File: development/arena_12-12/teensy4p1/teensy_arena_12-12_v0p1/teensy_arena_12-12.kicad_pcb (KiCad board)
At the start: 6 copper layers, 228.6 x 228.6 mm, 434 parts, among them J1 Barrel_Jack, J2 Conn_01x04, J3 Conn_01x04, J4 Barrel_Jack, P1 CONN15, P10 CONN15, P11 CONN15, P12 CONN15, P2 CONN15, P3 CONN15, P4 CONN15, P5 CONN15, P6 CONN15, P7 CONN15, P8 CONN15, P9 CONN15, Q1 MOSFET_NCHAN, SW1 SW_SPDT, U1 Teensy4.1, U10 TXB0108PW, U11 TXB0108PW, U12 TXB0108PW, U13 TXB0108PW, U14 TXB0108PW, U15 74LVC1G17, U16 74LVC1G17, U17 74LVC1G17, U18 74LVC1G17, U19 74LVC2G17, U2 74LVC2G17, U20 74LVC2G17, U21 74LVC2G17, U22 74LVC2G17, U23 74LVC2G17, U24 74LVC2G17, U25 74LVC2G17, U26 74LVC2G17, U27 74LVC2G17, U28 74LVC2G17, U29 74LVC2G17, U3 TXB0108PW, U30 74LVC2G17, U31 74LVC2G17, U32 74LVC2G17, U33 74LVC2G17, U34 74LVC2G17, U35 74LVC2G17, U36 74LVC2G17, U37 74LVC2G17, U38 74LVC2G17, U39 74LVC2G17, U4 TXB0108PW, U40 74LVC2G17, U41 74LVC2G17, U42 74LVC2G17, U43 74LVC2G17, U44 74LVC2G17, U45 74LVC2G17, U46 74LVC2G17, U47 74LVC2G17, U48 74LVC2G17, U49 74LVC2G17, U5 TXB0108PW, U50 74LVC2G17, U51 74LVC2G17, U52 74LVC2G17, U53 74LVC2G17, U54 74LVC2G17, U55 74LVC2G17, U56 74LVC2G17, U57 74LVC2G17, U58 74LVC2G17, U59 74LVC2G17, U6 TXB0108PW, U60 74LVC2G17, U61 74LVC2G17, U62 74LVC2G17, U63 74LVC2G17, U64 74LVC2G17, U65 74LVC2G17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

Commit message: Worked on 12-12 arena layout.
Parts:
- removed the Q1 at (284.3, 131.0)
- added R223: 68, Resistor_SMD:R_0603_1608Metric, F.Cu at (272.5, 172.7)
- added R224: 68, Resistor_SMD:R_0603_1608Metric, F.Cu at (257.2, 126.0)
- added R225: 68, Resistor_SMD:R_0603_1608Metric, F.Cu at (220.7, 93.3)
- added R226: 68, Resistor_SMD:R_0603_1608Metric, F.Cu at (172.7, 83.1)
- added R227: 68, Resistor_SMD:R_0603_1608Metric, F.Cu at (126.0, 98.4)
- added R228: 68, Resistor_SMD:R_0603_1608Metric, F.Cu at (93.3, 134.9)
- added R229: 68, Resistor_SMD:R_0603_1608Metric, F.Cu at (83.1, 182.9)
- added R230: 68, Resistor_SMD:R_0603_1608Metric, F.Cu at (98.4, 229.6)
- added R231: 68, Resistor_SMD:R_0603_1608Metric, F.Cu at (134.9, 262.3)
- added R232: 68, Resistor_SMD:R_0603_1608Metric, F.Cu at (182.9, 272.5)
- added R233: 68, Resistor_SMD:R_0603_1608Metric, F.Cu at (229.6, 257.2)
- added R234: 68, Resistor_SMD:R_0603_1608Metric, F.Cu at (262.3, 220.7)
- moved C50 361.1 mm to (272.5, 187.0), turned to 180 degrees
- moved C49 360.2 mm to (272.4, 181.6), turned to 180 degrees
- moved C48 359.4 mm to (272.4, 176.3), turned to 180 degrees
- moved C47 358.0 mm to (272.5, 169.0), turned to 180 degrees
- moved C91 349.8 mm to (264.2, 217.5), turned to 150 degrees
- moved R130 349.1 mm to (272.5, 178.0)
- moved R131 349.0 mm to (272.4, 180.0)
- moved C92 347.7 mm to (260.5, 223.9), turned to 150 degrees
- moved C93 346.0 mm to (257.9, 228.4), turned to 150 degrees
- moved C94 344.3 mm to (255.1, 233.1), turned to 150 degrees
- moved R128 342.0 mm to (272.5, 170.6)
- moved R127 341.9 mm to (272.5, 167.4)
- moved C87 341.6 mm to (232.7, 255.4), turned to 120 degrees
- moved C54 340.0 mm to (264.4, 138.5), turned to -150 degrees
- moved R215 337.6 mm to (265.0, 216.2), turned to -30 degrees
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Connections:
- P1 pad 6: /Level Shifters/PAN5V.MISO_0 -> /Panel Headers/HDR_MISO_0_P1
- P10 pad 6: /Level Shifters/PAN5V.MISO_1 -> /Panel Headers/HDR_MISO_1_P10
- P11 pad 6: /Level Shifters/PAN5V.MISO_1 -> /Panel Headers/HDR_MISO_1_P11
- P12 pad 6: /Level Shifters/PAN5V.MISO_1 -> /Panel Headers/HDR_MISO_1_P12
- P2 pad 6: /Level Shifters/PAN5V.MISO_0 -> /Panel Headers/HDR_MISO_0_P2
- P3 pad 6: /Level Shifters/PAN5V.MISO_0 -> /Panel Headers/HDR_MISO_0_P3
- P4 pad 6: /Level Shifters/PAN5V.MISO_0 -> /Panel Headers/HDR_MISO_0_P4
- P5 pad 6: /Level Shifters/PAN5V.MISO_0 -> /Panel Headers/HDR_MISO_0_P5
- P6 pad 6: /Level Shifters/PAN5V.MISO_0 -> /Panel Headers/HDR_MISO_0_P6
- P7 pad 6: /Level Shifters/PAN5V.MISO_1 -> /Panel Headers/HDR_MISO_1_P7
- P8 pad 6: /Level Shifters/PAN5V.MISO_1 -> /Panel Headers/HDR_MISO_1_P8
- P9 pad 6: /Level Shifters/PAN5V.MISO_1 -> /Panel Headers/HDR_MISO_1_P9
- U36 pad 1: /Level Shifters/PAN5V.SCK_0_P1 -> /Level Shifters/PAN5V.MOSI_0_P1
- U36 pad 3: /Level Shifters/PAN5V.MOSI_0_P1 -> /Level Shifters/PAN5V.SCK_0_P1
- U36 pad 4: Net-(R128-Pad2) -> Net-(R127-Pad2)
- U36 pad 6: Net-(R127-Pad2) -> Net-(R128-Pad2)
- U37 pad 1: /Level Shifters/PAN5V.CS_00_P1 -> /Level Shifters/PAN5V.CS_01_P1
- U37 pad 3: /Level Shifters/PAN5V.CS_01_P1 -> /Level Shifters/PAN5V.CS_00_P1
- U37 pad 4: Net-(R130-Pad2) -> Net-(R129-Pad2)
- U37 pad 6: Net-(R129-Pad2) -> Net-(R130-Pad2)
- U38 pad 1: /Level Shifters/PAN5V.CS_02_P1 -> /Level Shifters/PAN5V.CS_03_P1
- U38 pad 3: /Level Shifters/PAN5V.CS_03_P1 -> /Level Shifters/PAN5V.CS_02_P1
- U38 pad 4: Net-(R132-Pad2) -> Net-(R131-Pad2)
- U38 pad 6: Net-(R131-Pad2) -> Net-(R132-Pad2)
- U39 pad 1: /Level Shifters/PAN5V.CS_04_P1 -> /Level Shifters/PAN5V.EXT_INT
- U39 pad 3: /Level Shifters/PAN5V.EXT_INT -> /Level Shifters/PAN5V.CS_04_P1
- U39 pad 4: Net-(R134-Pad2) -> Net-(R133-Pad2)
- U39 pad 6: Net-(R133-Pad2) -> Net-(R134-Pad2)
- U40 pad 1: /Level Shifters/PAN5V.SCK_0_P2 -> /Level Shifters/PAN5V.MOSI_0_P2
- U40 pad 3: /Level Shifters/PAN5V.MOSI_0_P2 -> /Level Shifters/PAN5V.SCK_0_P2
- U40 pad 4: Net-(R136-Pad2) -> Net-(R135-Pad2)
- U40 pad 6: Net-(R135-Pad2) -> Net-(R136-Pad2)
- U41 pad 1: /Level Shifters/PAN5V.CS_05_P2 -> /Level Shifters/PAN5V.CS_06_P2
- U41 pad 3: /Level Shifters/PAN5V.CS_06_P2 -> /Level Shifters/PAN5V.CS_05_P2
- U41 pad 4: Net-(R138-Pad2) -> Net-(R137-Pad2)
- U41 pad 6: Net-(R137-Pad2) -> Net-(R138-Pad2)
- U42 pad 1: /Level Shifters/PAN5V.CS_07_P2 -> /Level Shifters/PAN5V.CS_08_P2
- U42 pad 3: /Level Shifters/PAN5V.CS_08_P2 -> /Level Shifters/PAN5V.CS_07_P2
- U42 pad 4: Net-(R140-Pad2) -> Net-(R139-Pad2)
- U42 pad 6: Net-(R139-Pad2) -> Net-(R140-Pad2)
- U43 pad 1: /Level Shifters/PAN5V.CS_09_P2 -> /Level Shifters/PAN5V.EXT_INT
- U43 pad 3: /Level Shifters/PAN5V.EXT_INT -> /Level Shifters/PAN5V.CS_09_P2
- U43 pad 4: Net-(R142-Pad2) -> Net-(R141-Pad2)
- U43 pad 6: Net-(R141-Pad2) -> Net-(R142-Pad2)
- U44 pad 1: /Level Shifters/PAN5V.SCK_0_P3 -> /Level Shifters/PAN5V.MOSI_0_P3
- U44 pad 3: /Level Shifters/PAN5V.MOSI_0_P3 -> /Level Shifters/PAN5V.SCK_0_P3
- U44 pad 4: Net-(R144-Pad2) -> Net-(R143-Pad2)
- U44 pad 6: Net-(R143-Pad2) -> Net-(R144-Pad2)
- U45 pad 1: /Level Shifters/PAN5V.CS_10_P3 -> /Level Shifters/PAN5V.CS_11_P3
- U45 pad 3: /Level Shifters/PAN5V.CS_11_P3 -> /Level Shifters/PAN5V.CS_10_P3
- U45 pad 4: Net-(R146-Pad2) -> Net-(R145-Pad2)
- U45 pad 6: Net-(R145-Pad2) -> Net-(R146-Pad2)
- U46 pad 1: /Level Shifters/PAN5V.CS_12_P3 -> /Level Shifters/PAN5V.CS_13_P3
- U46 pad 3: /Level Shifters/PAN5V.CS_13_P3 -> /Level Shifters/PAN5V.CS_12_P3
- U46 pad 4: Net-(R148-Pad2) -> Net-(R147-Pad2)
- U46 pad 6: Net-(R147-Pad2) -> Net-(R148-Pad2)
- U47 pad 1: /Level Shifters/PAN5V.CS_14_P3 -> /Level Shifters/PAN5V.EXT_INT
- U47 pad 3: /Level Shifters/PAN5V.EXT_INT -> /Level Shifters/PAN5V.CS_14_P3
- U47 pad 4: Net-(R150-Pad2) -> Net-(R149-Pad2)
- U47 pad 6: Net-(R149-Pad2) -> Net-(R150-Pad2)
- U48 pad 1: /Level Shifters/PAN5V.SCK_0_P4 -> /Level Shifters/PAN5V.MOSI_0_P4
- U48 pad 3: /Level Shifters/PAN5V.MOSI_0_P4 -> /Level Shifters/PAN5V.SCK_0_P4
- U48 pad 4: Net-(R152-Pad2) -> Net-(R151-Pad2)
- U48 pad 6: Net-(R151-Pad2) -> Net-(R152-Pad2)
- U49 pad 1: /Level Shifters/PAN5V.CS_15_P4 -> /Level Shifters/PAN5V.CS_16_P4
- U49 pad 3: /Level Shifters/PAN5V.CS_16_P4 -> /Level Shifters/PAN5V.CS_15_P4
- U49 pad 4: Net-(R154-Pad2) -> Net-(R153-Pad2)
- U49 pad 6: Net-(R153-Pad2) -> Net-(R154-Pad2)
- U50 pad 1: /Level Shifters/PAN5V.CS_17_P4 -> /Level Shifters/PAN5V.CS_18_P4
- U50 pad 3: /Level Shifters/PAN5V.CS_18_P4 -> /Level Shifters/PAN5V.CS_17_P4
- U50 pad 4: Net-(R156-Pad2) -> Net-(R155-Pad2)
- U50 pad 6: Net-(R155-Pad2) -> Net-(R156-Pad2)
- U51 pad 1: /Level Shifters/PAN5V.CS_19_P4 -> /Level Shifters/PAN5V.EXT_INT
- U51 pad 3: /Level Shifters/PAN5V.EXT_INT -> /Level Shifters/PAN5V.CS_19_P4
- U51 pad 4: Net-(R158-Pad2) -> Net-(R157-Pad2)
- U51 pad 6: Net-(R157-Pad2) -> Net-(R158-Pad2)
- U52 pad 1: /Level Shifters/PAN5V.SCK_0_P5 -> /Level Shifters/PAN5V.MOSI_0_P5
- U52 pad 3: /Level Shifters/PAN5V.MOSI_0_P5 -> /Level Shifters/PAN5V.SCK_0_P5
- U52 pad 4: Net-(R160-Pad2) -> Net-(R159-Pad2)
- U52 pad 6: Net-(R159-Pad2) -> Net-(R160-Pad2)
- U53 pad 1: /Level Shifters/PAN5V.CS_20_P5 -> /Level Shifters/PAN5V.CS_21_P5
- U53 pad 3: /Level Shifters/PAN5V.CS_21_P5 -> /Level Shifters/PAN5V.CS_20_P5
- U53 pad 4: Net-(R162-Pad2) -> Net-(R161-Pad2)
- U53 pad 6: Net-(R161-Pad2) -> Net-(R162-Pad2)
- U54 pad 1: /Level Shifters/PAN5V.CS_22_P5 -> /Level Shifters/PAN5V.CS_23_P5
- U54 pad 3: /Level Shifters/PAN5V.CS_23_P5 -> /Level Shifters/PAN5V.CS_22_P5
- U54 pad 4: Net-(R164-Pad2) -> Net-(R163-Pad2)
- U54 pad 6: Net-(R163-Pad2) -> Net-(R164-Pad2)
- U55 pad 1: /Level Shifters/PAN5V.CS_24_P5 -> /Level Shifters/PAN5V.EXT_INT
- U55 pad 3: /Level Shifters/PAN5V.EXT_INT -> /Level Shifters/PAN5V.CS_24_P5
- U55 pad 4: Net-(R166-Pad2) -> Net-(R165-Pad2)
- U55 pad 6: Net-(R165-Pad2) -> Net-(R166-Pad2)
- U56 pad 1: /Level Shifters/PAN5V.SCK_0_P6 -> /Level Shifters/PAN5V.MOSI_0_P6
- U56 pad 3: /Level Shifters/PAN5V.MOSI_0_P6 -> /Level Shifters/PAN5V.SCK_0_P6
- U56 pad 4: Net-(R168-Pad2) -> Net-(R167-Pad2)
- U56 pad 6: Net-(R167-Pad2) -> Net-(R168-Pad2)
- U57 pad 1: /Level Shifters/PAN5V.CS_25_P6 -> /Level Shifters/PAN5V.CS_26_P6
- U57 pad 3: /Level Shifters/PAN5V.CS_26_P6 -> /Level Shifters/PAN5V.CS_25_P6
- U57 pad 4: Net-(R170-Pad2) -> Net-(R169-Pad2)
- U57 pad 6: Net-(R169-Pad2) -> Net-(R170-Pad2)
- U58 pad 1: /Level Shifters/PAN5V.CS_27_P6 -> /Level Shifters/PAN5V.CS_28_P6
- U58 pad 3: /Level Shifters/PAN5V.CS_28_P6 -> /Level Shifters/PAN5V.CS_27_P6
- U58 pad 4: Net-(R172-Pad2) -> Net-(R171-Pad2)
- U58 pad 6: Net-(R171-Pad2) -> Net-(R172-Pad2)
- U59 pad 1: /Level Shifters/PAN5V.CS_29_P6 -> /Level Shifters/PAN5V.EXT_INT
- U59 pad 3: /Level Shifters/PAN5V.EXT_INT -> /Level Shifters/PAN5V.CS_29_P6
- U59 pad 4: Net-(R174-Pad2) -> Net-(R173-Pad2)
- U59 pad 6: Net-(R173-Pad2) -> Net-(R174-Pad2)
- U60 pad 1: /Level Shifters/PAN5V.SCK_1_P7 -> /Level Shifters/PAN5V.MOSI_1_P7
- U60 pad 3: /Level Shifters/PAN5V.MOSI_1_P7 -> /Level Shifters/PAN5V.SCK_1_P7
- U60 pad 4: Net-(R176-Pad2) -> Net-(R175-Pad2)
- U60 pad 6: Net-(R175-Pad2) -> Net-(R176-Pad2)
- U61 pad 1: /Level Shifters/PAN5V.CS_00_P7 -> /Level Shifters/PAN5V.CS_01_P7
- U61 pad 3: /Level Shifters/PAN5V.CS_01_P7 -> /Level Shifters/PAN5V.CS_00_P7
- U61 pad 4: Net-(R178-Pad2) -> Net-(R177-Pad2)
- U61 pad 6: Net-(R177-Pad2) -> Net-(R178-Pad2)
- U62 pad 1: /Level Shifters/PAN5V.CS_02_P7 -> /Level Shifters/PAN5V.CS_03_P7
- U62 pad 3: /Level Shifters/PAN5V.CS_03_P7 -> /Level Shifters/PAN5V.CS_02_P7
- U62 pad 4: Net-(R180-Pad2) -> Net-(R179-Pad2)
- U62 pad 6: Net-(R179-Pad2) -> Net-(R180-Pad2)
- U63 pad 1: /Level Shifters/PAN5V.CS_04_P7 -> /Level Shifters/PAN5V.EXT_INT
- U63 pad 3: /Level Shifters/PAN5V.EXT_INT -> /Level Shifters/PAN5V.CS_04_P7
- U63 pad 4: Net-(R182-Pad2) -> Net-(R181-Pad2)
- U63 pad 6: Net-(R181-Pad2) -> Net-(R182-Pad2)
- U64 pad 1: /Level Shifters/PAN5V.SCK_1_P8 -> /Level Shifters/PAN5V.MOSI_1_P8
- U64 pad 3: /Level Shifters/PAN5V.MOSI_1_P8 -> /Level Shifters/PAN5V.SCK_1_P8
- U64 pad 4: Net-(R184-Pad2) -> Net-(R183-Pad2)
- U64 pad 6: Net-(R183-Pad2) -> Net-(R184-Pad2)
- U65 pad 1: /Level Shifters/PAN5V.CS_05_P8 -> /Level Shifters/PAN5V.CS_06_P8
- U65 pad 3: /Level Shifters/PAN5V.CS_06_P8 -> /Level Shifters/PAN5V.CS_05_P8
- U65 pad 4: Net-(R186-Pad2) -> Net-(R185-Pad2)
- U65 pad 6: Net-(R185-Pad2) -> Net-(R186-Pad2)
- U66 pad 1: /Level Shifters/PAN5V.CS_07_P8 -> /Level Shifters/PAN5V.CS_08_P8
- U66 pad 3: /Level Shifters/PAN5V.CS_08_P8 -> /Level Shifters/PAN5V.CS_07_P8
- U66 pad 4: Net-(R188-Pad2) -> Net-(R187-Pad2)
- U66 pad 6: Net-(R187-Pad2) -> Net-(R188-Pad2)
- U67 pad 1: /Level Shifters/PAN5V.CS_09_P8 -> /Level Shifters/PAN5V.EXT_INT
- U67 pad 3: /Level Shifters/PAN5V.EXT_INT -> /Level Shifters/PAN5V.CS_09_P8
- U67 pad 4: Net-(R190-Pad2) -> Net-(R189-Pad2)
- U67 pad 6: Net-(R189-Pad2) -> Net-(R190-Pad2)
- U68 pad 1: /Level Shifters/PAN5V.SCK_1_P9 -> /Level Shifters/PAN5V.MOSI_1_P9
- U68 pad 3: /Level Shifters/PAN5V.MOSI_1_P9 -> /Level Shifters/PAN5V.SCK_1_P9
- U68 pad 4: Net-(R192-Pad2) -> Net-(R191-Pad2)
- U68 pad 6: Net-(R191-Pad2) -> Net-(R192-Pad2)
- U69 pad 1: /Level Shifters/PAN5V.CS_10_P9 -> /Level Shifters/PAN5V.CS_11_P9
- U69 pad 3: /Level Shifters/PAN5V.CS_11_P9 -> /Level Shifters/PAN5V.CS_10_P9
- U69 pad 4: Net-(R194-Pad2) -> Net-(R193-Pad2)
- U69 pad 6: Net-(R193-Pad2) -> Net-(R194-Pad2)
- U70 pad 1: /Level Shifters/PAN5V.CS_12_P9 -> /Level Shifters/PAN5V.CS_13_P9
- U70 pad 3: /Level Shifters/PAN5V.CS_13_P9 -> /Level Shifters/PAN5V.CS_12_P9
- U70 pad 4: Net-(R196-Pad2) -> Net-(R195-Pad2)
- U70 pad 6: Net-(R195-Pad2) -> Net-(R196-Pad2)
- U71 pad 1: /Level Shifters/PAN5V.CS_14_P9 -> /Level Shifters/PAN5V.EXT_INT
- U71 pad 3: /Level Shifters/PAN5V.EXT_INT -> /Level Shifters/PAN5V.CS_14_P9
- U71 pad 4: Net-(R198-Pad2) -> Net-(R197-Pad2)
- U71 pad 6: Net-(R197-Pad2) -> Net-(R198-Pad2)
- U72 pad 1: /Level Shifters/PAN5V.SCK_1_P10 -> /Level Shifters/PAN5V.MOSI_1_P10
- U72 pad 3: /Level Shifters/PAN5V.MOSI_1_P10 -> /Level Shifters/PAN5V.SCK_1_P10
- U72 pad 4: Net-(R200-Pad2) -> Net-(R199-Pad2)
- U72 pad 6: Net-(R199-Pad2) -> Net-(R200-Pad2)
- U73 pad 1: /Level Shifters/PAN5V.CS_15_P10 -> /Level Shifters/PAN5V.CS_16_P10
- U73 pad 3: /Level Shifters/PAN5V.CS_16_P10 -> /Level Shifters/PAN5V.CS_15_P10
- U73 pad 4: Net-(R202-Pad2) -> Net-(R201-Pad2)
- U73 pad 6: Net-(R201-Pad2) -> Net-(R202-Pad2)
- U74 pad 1: /Level Shifters/PAN5V.CS_17_P10 -> /Level Shifters/PAN5V.CS_18_P10
- U74 pad 3: /Level Shifters/PAN5V.CS_18_P10 -> /Level Shifters/PAN5V.CS_17_P10
- U74 pad 4: Net-(R204-Pad2) -> Net-(R203-Pad2)
- U74 pad 6: Net-(R203-Pad2) -> Net-(R204-Pad2)
- U75 pad 1: /Level Shifters/PAN5V.CS_19_P10 -> /Level Shifters/PAN5V.EXT_INT
- U75 pad 3: /Level Shifters/PAN5V.EXT_INT -> /Level Shifters/PAN5V.CS_19_P10
- U75 pad 4: Net-(R206-Pad2) -> Net-(R205-Pad2)
- U75 pad 6: Net-(R205-Pad2) -> Net-(R206-Pad2)
- U76 pad 1: /Level Shifters/PAN5V.SCK_1_P11 -> /Level Shifters/PAN5V.MOSI_1_P11
- U76 pad 3: /Level Shifters/PAN5V.MOSI_1_P11 -> /Level Shifters/PAN5V.SCK_1_P11
- U76 pad 4: Net-(R208-Pad2) -> Net-(R207-Pad2)
- U76 pad 6: Net-(R207-Pad2) -> Net-(R208-Pad2)
- U77 pad 1: /Level Shifters/PAN5V.CS_20_P11 -> /Level Shifters/PAN5V.CS_21_P11
- U77 pad 3: /Level Shifters/PAN5V.CS_21_P11 -> /Level Shifters/PAN5V.CS_20_P11
- U77 pad 4: Net-(R210-Pad2) -> Net-(R209-Pad2)
- U77 pad 6: Net-(R209-Pad2) -> Net-(R210-Pad2)
- U78 pad 1: /Level Shifters/PAN5V.CS_22_P11 -> /Level Shifters/PAN5V.CS_23_P11
- U78 pad 3: /Level Shifters/PAN5V.CS_23_P11 -> /Level Shifters/PAN5V.CS_22_P11
- U78 pad 4: Net-(R212-Pad2) -> Net-(R211-Pad2)
- U78 pad 6: Net-(R211-Pad2) -> Net-(R212-Pad2)
- U79 pad 1: /Level Shifters/PAN5V.CS_24_P11 -> /Level Shifters/PAN5V.EXT_INT
- U79 pad 3: /Level Shifters/PAN5V.EXT_INT -> /Level Shifters/PAN5V.CS_24_P11
- U79 pad 4: Net-(R214-Pad2) -> Net-(R213-Pad2)
- U79 pad 6: Net-(R213-Pad2) -> Net-(R214-Pad2)
- U80 pad 1: /Level Shifters/PAN5V.SCK_1_P12 -> /Level Shifters/PAN5V.MOSI_1_P12
- U80 pad 3: /Level Shifters/PAN5V.MOSI_1_P12 -> /Level Shifters/PAN5V.SCK_1_P12
- U80 pad 4: Net-(R216-Pad2) -> Net-(R215-Pad2)
- U80 pad 6: Net-(R215-Pad2) -> Net-(R216-Pad2)
- U81 pad 1: /Level Shifters/PAN5V.CS_25_P12 -> /Level Shifters/PAN5V.CS_26_P12
- U81 pad 3: /Level Shifters/PAN5V.CS_26_P12 -> /Level Shifters/PAN5V.CS_25_P12
- U81 pad 4: Net-(R218-Pad2) -> Net-(R217-Pad2)
- U81 pad 6: Net-(R217-Pad2) -> Net-(R218-Pad2)
- U82 pad 1: /Level Shifters/PAN5V.CS_27_P12 -> /Level Shifters/PAN5V.CS_28_P12
- U82 pad 3: /Level Shifters/PAN5V.CS_28_P12 -> /Level Shifters/PAN5V.CS_27_P12
- U82 pad 4: Net-(R220-Pad2) -> Net-(R219-Pad2)
- U82 pad 6: Net-(R219-Pad2) -> Net-(R220-Pad2)
- U83 pad 1: /Level Shifters/PAN5V.CS_29_P12 -> /Level Shifters/PAN5V.EXT_INT
- U83 pad 3: /Level Shifters/PAN5V.EXT_INT -> /Level Shifters/PAN5V.CS_29_P12
- U83 pad 4: Net-(R222-Pad2) -> Net-(R221-Pad2)
- U83 pad 6: Net-(R221-Pad2) -> Net-(R222-Pad2)

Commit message: Finished preliminary layout for new 12-12 teensy 4.1 arena.
Includes source termination resistors and schmitt trigger buffers.
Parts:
- C1, C10, C11, C12, C13, C14, C15, C16, C17, C18, C19, C2, C20, C21, C22, C23, C24, C25, C26, C27, C28, C29, C3, C30, C31, C32, C33, C34, C35, C36, C37, C38, C39, C4, C40, C41, C42, C43, C44, C45, C46, C47, C48, C49, C5, C50, C51, C52, C53, C54, C55, C56, C57, C58, C59, C6, C60, C61, C62, C63, C64, C65, C66, C67, C68, C69, C7, C70, C71, C72, C73, C74, C75, C76, C77, C78, C79, C8, C80, C81, C82, C83, C84, C85, C86, C87, C88, C89, C9, C90, C91, C92, C93, C94: footprint Capacitor_SMD:C_0603_1608Metric -> Capacitor_SMD:C_0402_1005Metric
- R10, R100, R101, R102, R103, R104, R105, R106, R107, R108, R109, R11, R110, R111, R112, R113, R114, R115, R116, R117, R118, R119, R12, R120, R121, R122, R123, R124, R125, R126, R127, R128, R129, R13, R130, R131, R132, R133, R134, R135, R136, R137, R138, R139, R14, R140, R141, R142, R143, R144, R145, R146, R147, R148, R149, R15, R150, R151, R152, R153, R154, R155, R156, R157, R158, R159, R16, R160, R161, R162, R163, R164, R165, R166, R167, R168, R169, R17, R170, R171, R172, R173, R174, R175, R176, R177, R178, R179, R18, R180, R181, R182, R183, R184, R185, R186, R187, R188, R189, R19, R190, R191, R192, R193, R194, R195, R196, R197, R198, R199, R20, R200, R201, R202, R203, R204, R205, R206, R207, R208, R209, R21, R210, R211, R212, R213, R214, R215, R216, R217, R218, R219, R22, R220, R221, R222, R223, R224, R225, R226, R227, R228, R229, R23, R230, R231, R232, R233, R234, R24, R25, R26, R27, R28, R29, R3, R30, R31, R32, R33, R34, R35, R36, R37, R38, R39, R4, R40, R41, R42, R43, R44, R45, R46, R47, R48, R49, R5, R50, R51, R52, R53, R54, R55, R56, R57, R58, R59, R6, R60, R61, R62, R63, R64, R65, R66, R67, R68, R69, R7, R70, R71, R72, R73, R74, R75, R76, R77, R78, R79, R8, R80, R81, R82, R83, R84, R85, R86, R87, R88, R89, R9, R90, R91, R92, R93, R94, R95, R96, R97, R98, R99: footprint Resistor_SMD:R_0603_1608Metric -> Resistor_SMD:R_0402_1005Metric
- moved C33 368.8 mm to (285.8, 235.1), turned to 90 degrees
- moved C32 366.2 mm to (282.3, 235.1), turned to 90 degrees
- moved C12 365.7 mm to (282.3, 232.1), turned to -90 degrees
- moved C13 361.6 mm to (281.1, 221.5), turned to 90 degrees
- moved C10 361.2 mm to (282.9, 203.5), turned to -90 degrees
- moved C4 360.6 mm to (265.9, 246.7), turned to -90 degrees
- moved C31 358.7 mm to (286.5, 206.3), turned to 90 degrees
- moved C11 358.0 mm to (281.8, 193.1), turned to 90 degrees
- moved C5 357.2 mm to (266.8, 236.8), turned to 90 degrees
- moved C30 355.5 mm to (282.9, 206.3), turned to 90 degrees
- moved C27 351.2 mm to (267.0, 246.7), turned to -90 degrees
- moved R78 350.1 mm to (288.3, 221.5), turned to -90 degrees
- moved R77 349.8 mm to (287.2, 221.5), turned to -90 degrees
- moved U8 349.7 mm to (284.5, 227.1), turned to 90 degrees
- moved R76 349.4 mm to (286.2, 221.5), turned to -90 degrees
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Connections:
- U35 pad 1: /Level Shifters/PAN5V.MISO_0 -> /Level Shifters/PAN5V.MISO_1
- U35 pad 3: /Level Shifters/PAN5V.MISO_1 -> /Level Shifters/PAN5V.MISO_0
- U35 pad 4: Net-(U14-B8) -> Net-(U14-B7)
- U35 pad 6: Net-(U14-B7) -> Net-(U14-B8)

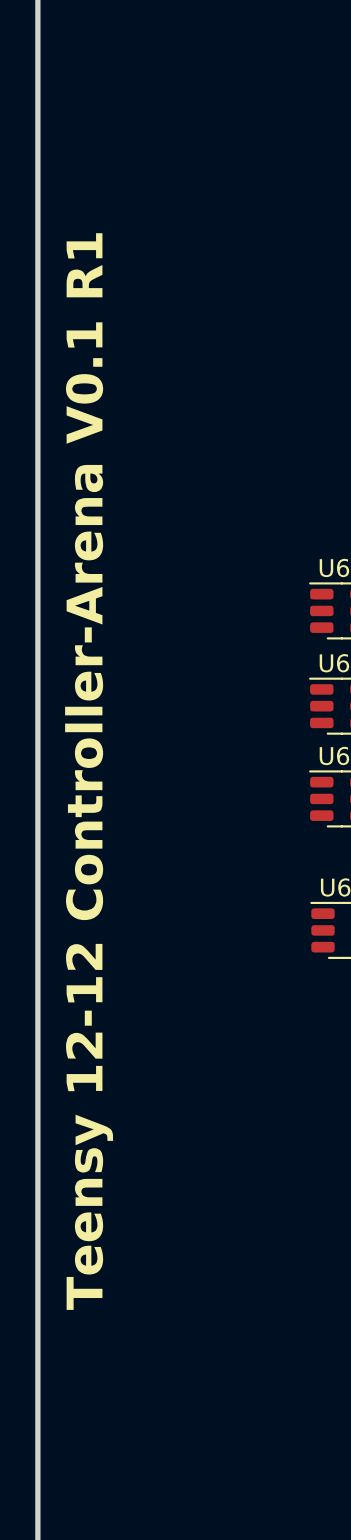
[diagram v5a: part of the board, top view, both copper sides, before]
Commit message: Added for 12-12 arena top.
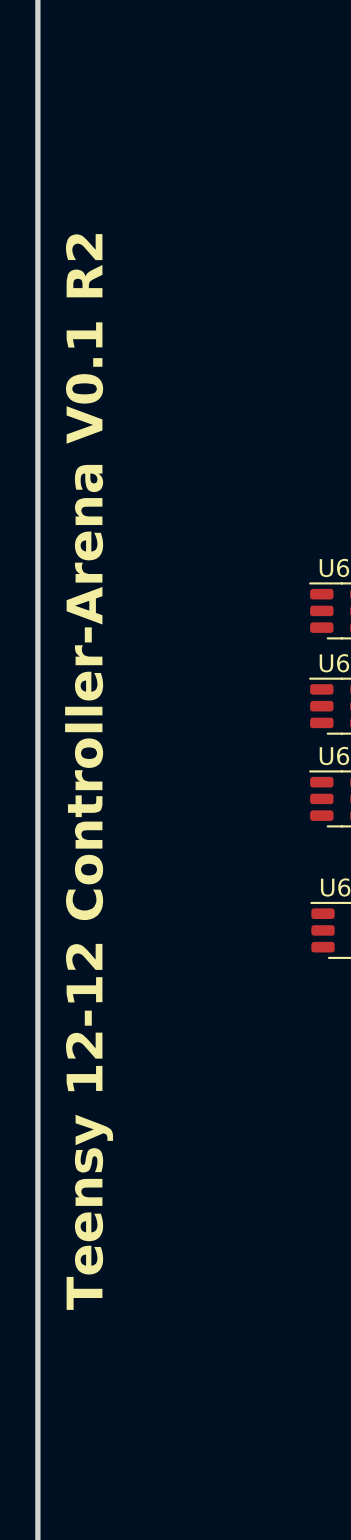
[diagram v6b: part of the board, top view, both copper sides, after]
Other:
- board text added: "Teensy 12-12 Controller-Arena V0.1 R2"
- board text removed: "Teensy 12-12 Controller-Arena V0.1 R1"

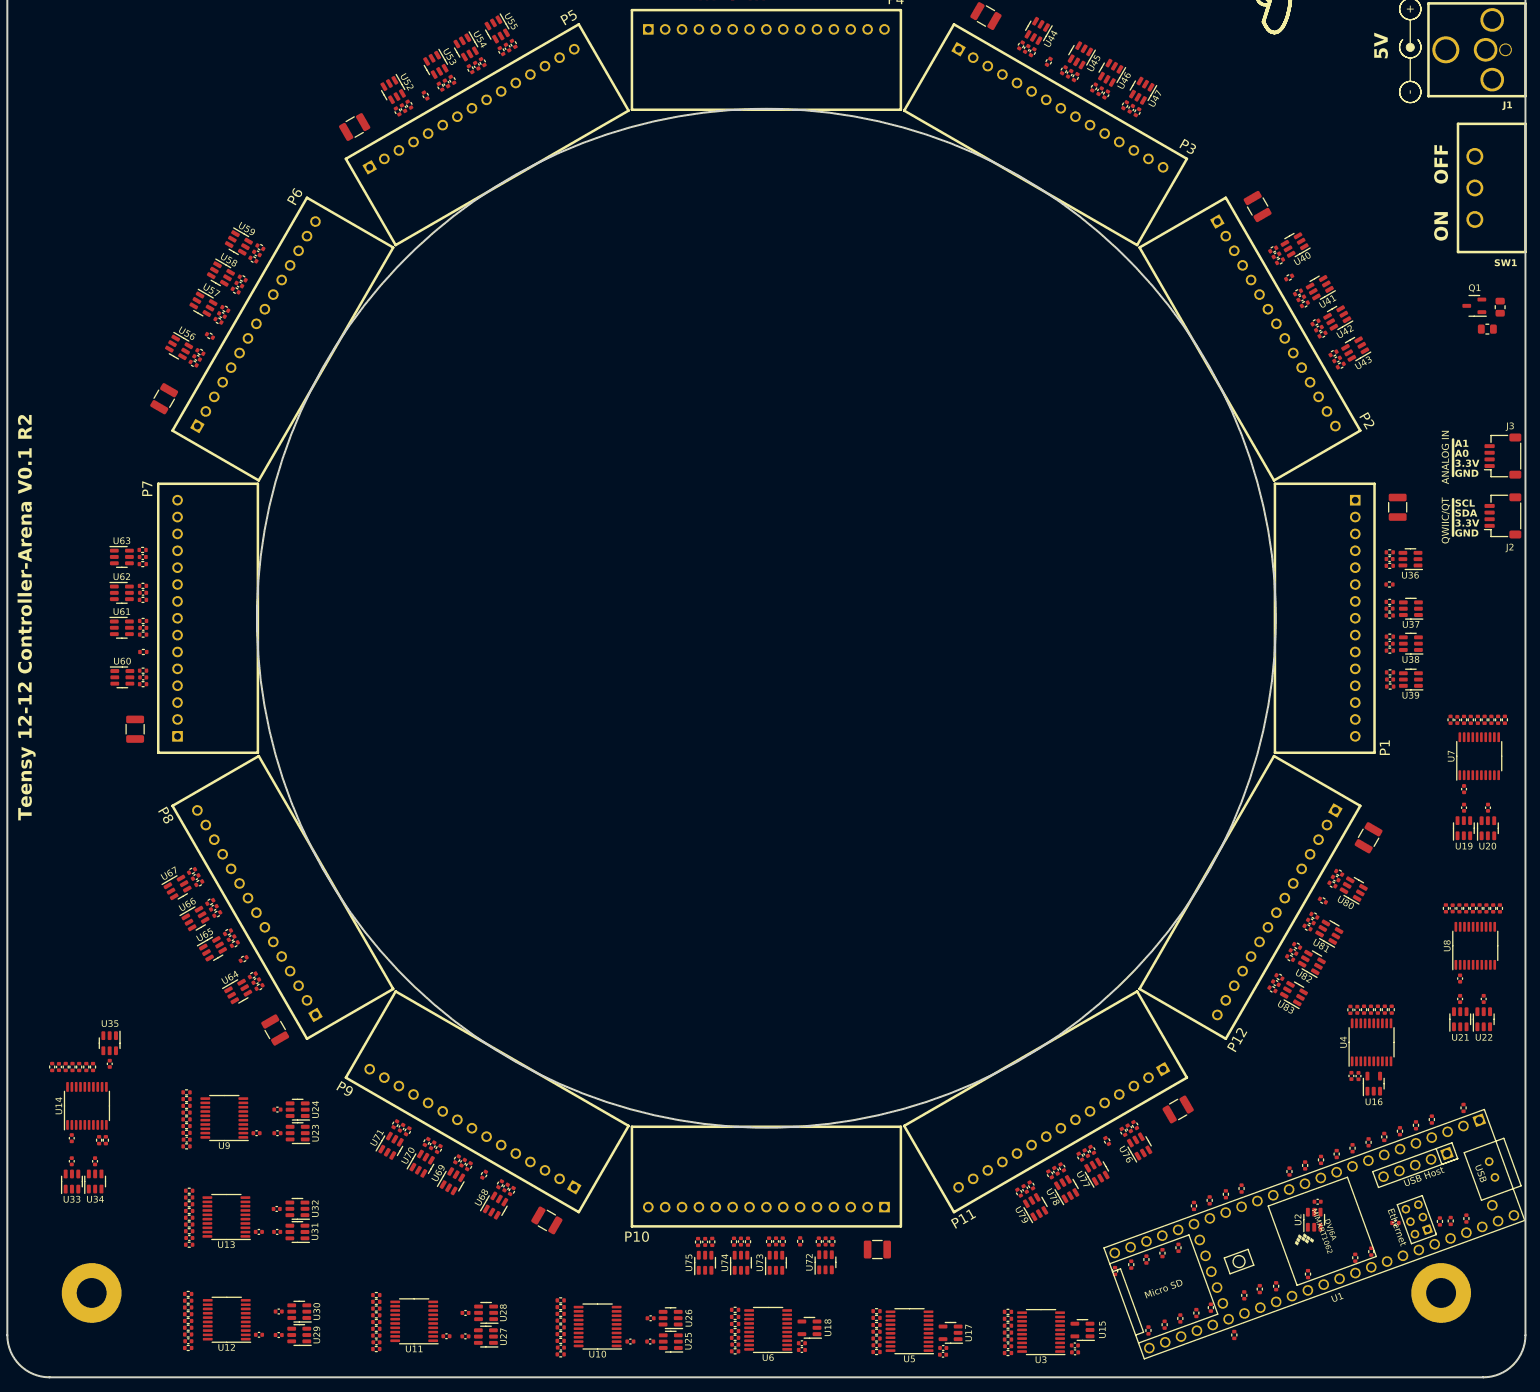
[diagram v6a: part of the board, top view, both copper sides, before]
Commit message: Worked on prelimnary hand routing of 12-12 teensy 4.1 arena.
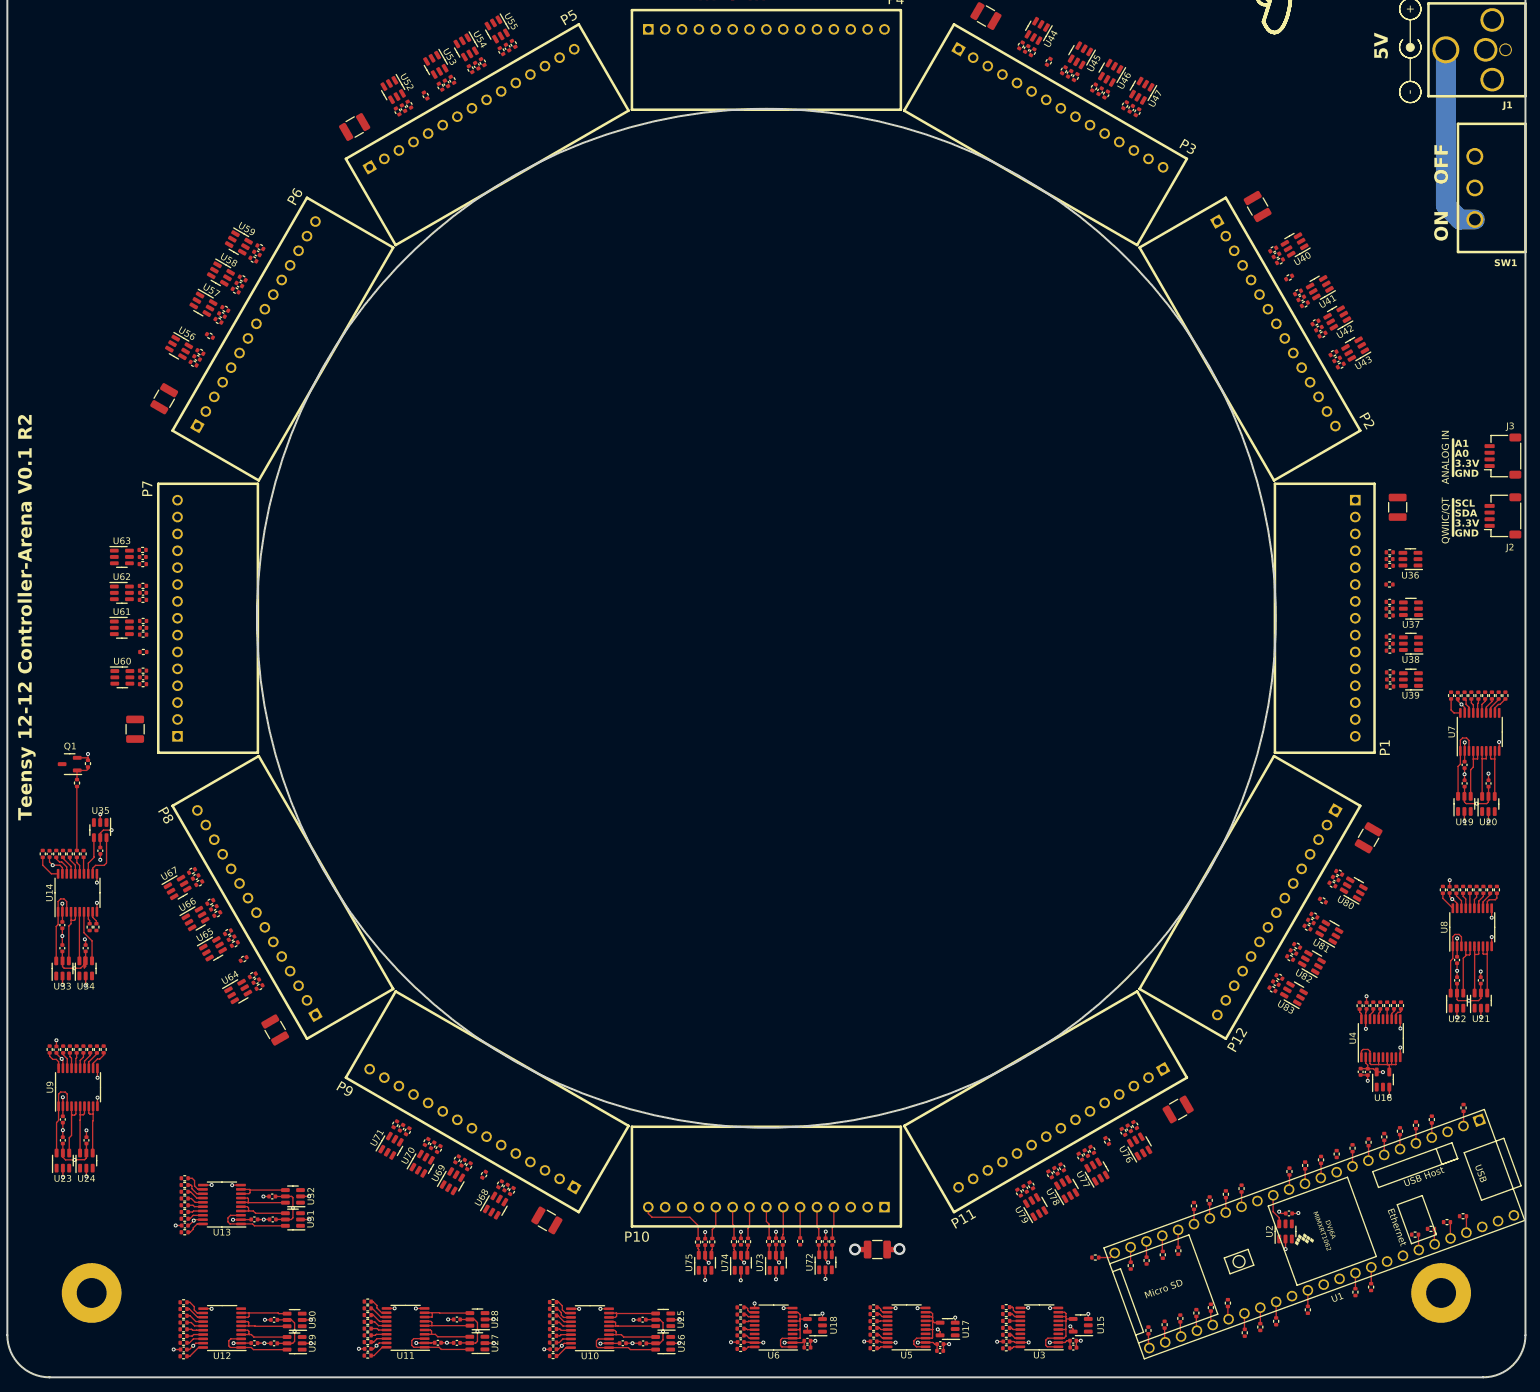
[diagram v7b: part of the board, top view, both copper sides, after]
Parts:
- R1, R2: footprint Resistor_SMD:R_0805_2012Metric -> Resistor_SMD:R_0402_1005Metric
- U1: footprint teensy:Teensy41 -> teensy:Teensy41_outer_only
- moved R2 223.5 mm to (75.6, 199.7)
- moved R1 223.1 mm to (74.0, 202.6), turned to -90 degrees
- moved Q1 222.5 mm to (72.9, 199.8)
- moved U23 35.6 mm to (71.9, 259.5), turned to 90 degrees
- moved U24 32.7 mm to (75.4, 259.5), turned to 90 degrees
- moved C34 32.3 mm to (71.9, 256.4), turned to 90 degrees
- moved C44 32.1 mm to (71.8, 227.5)
- moved C45 32.1 mm to (75.3, 227.5)
- moved C46 32.1 mm to (77.5, 212.8)
- moved R122 32.1 mm to (72.9, 213.3)
- moved R123 32.1 mm to (74.0, 213.3)
- moved R124 32.1 mm to (75.0, 213.3)
- moved U14 32.1 mm to (74.1, 219.1)
- moved U34 32.1 mm to (75.3, 230.5)
- moved C24 32.1 mm to (71.8, 224.0)
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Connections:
- U21 pad 1: /Level Shifters/PAN3V.CS_04 -> /Level Shifters/PAN3V.CS_06
- U21 pad 3: /Level Shifters/PAN3V.CS_05 -> /Level Shifters/PAN3V.CS_07
- U21 pad 4: Net-(U8-A3) -> Net-(U8-A7)
- U21 pad 6: Net-(U8-A1) -> Net-(U8-A5)
- U22 pad 1: /Level Shifters/PAN3V.CS_06 -> /Level Shifters/PAN3V.CS_04
- U22 pad 3: /Level Shifters/PAN3V.CS_07 -> /Level Shifters/PAN3V.CS_05
- U22 pad 4: Net-(U8-A7) -> Net-(U8-A3)
- U22 pad 6: Net-(U8-A5) -> Net-(U8-A1)
- U25 pad 1: /Level Shifters/PAN3V.CS_12 -> /Level Shifters/PAN3V.CS_14
- U25 pad 3: /Level Shifters/PAN3V.CS_13 -> /Level Shifters/PAN3V.CS_15
- U25 pad 4: Net-(U10-A3) -> Net-(U10-A7)
- U25 pad 6: Net-(U10-A1) -> Net-(U10-A5)
- U26 pad 1: /Level Shifters/PAN3V.CS_14 -> /Level Shifters/PAN3V.CS_12
- U26 pad 3: /Level Shifters/PAN3V.CS_15 -> /Level Shifters/PAN3V.CS_13
- U26 pad 4: Net-(U10-A7) -> Net-(U10-A3)
- U26 pad 6: Net-(U10-A5) -> Net-(U10-A1)
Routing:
- net +3.3V: track 0.00 -> 142.4 mm, vias 0 -> 40
- net GND: track 0.00 -> 98.7 mm, vias 0 -> 75
- net +5V: track 0.00 -> 36.7 mm, vias 0 -> 13
- net /Power/SW_5V: track 0.00 -> 28.7 mm
- net Net-(U3-A1): track 0.00 -> 15.1 mm
- net Net-(U5-A1): track 0.00 -> 14.7 mm
- net Net-(U6-A1): track 0.00 -> 14.1 mm
- net Net-(U4-A1): track 0.00 -> 14.0 mm
- net Net-(U9-A1): track 0.00 -> 12.4 mm
- net Net-(U14-A1): track 0.00 -> 12.2 mm
- net Net-(U10-A1): track 0.00 -> 11.9 mm
- net Net-(U7-A1): track 0.00 -> 11.8 mm
- net Net-(U11-A1): track 0.00 -> 11.8 mm
- net Net-(U12-A1): track 0.00 -> 11.7 mm
- net Net-(U8-A1): track 0.00 -> 11.7 mm
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- added copper zone on In3.Cu, net +3.3V
- added copper zone on In4.Cu, net GND
